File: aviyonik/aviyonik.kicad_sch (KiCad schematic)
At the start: 0 parts

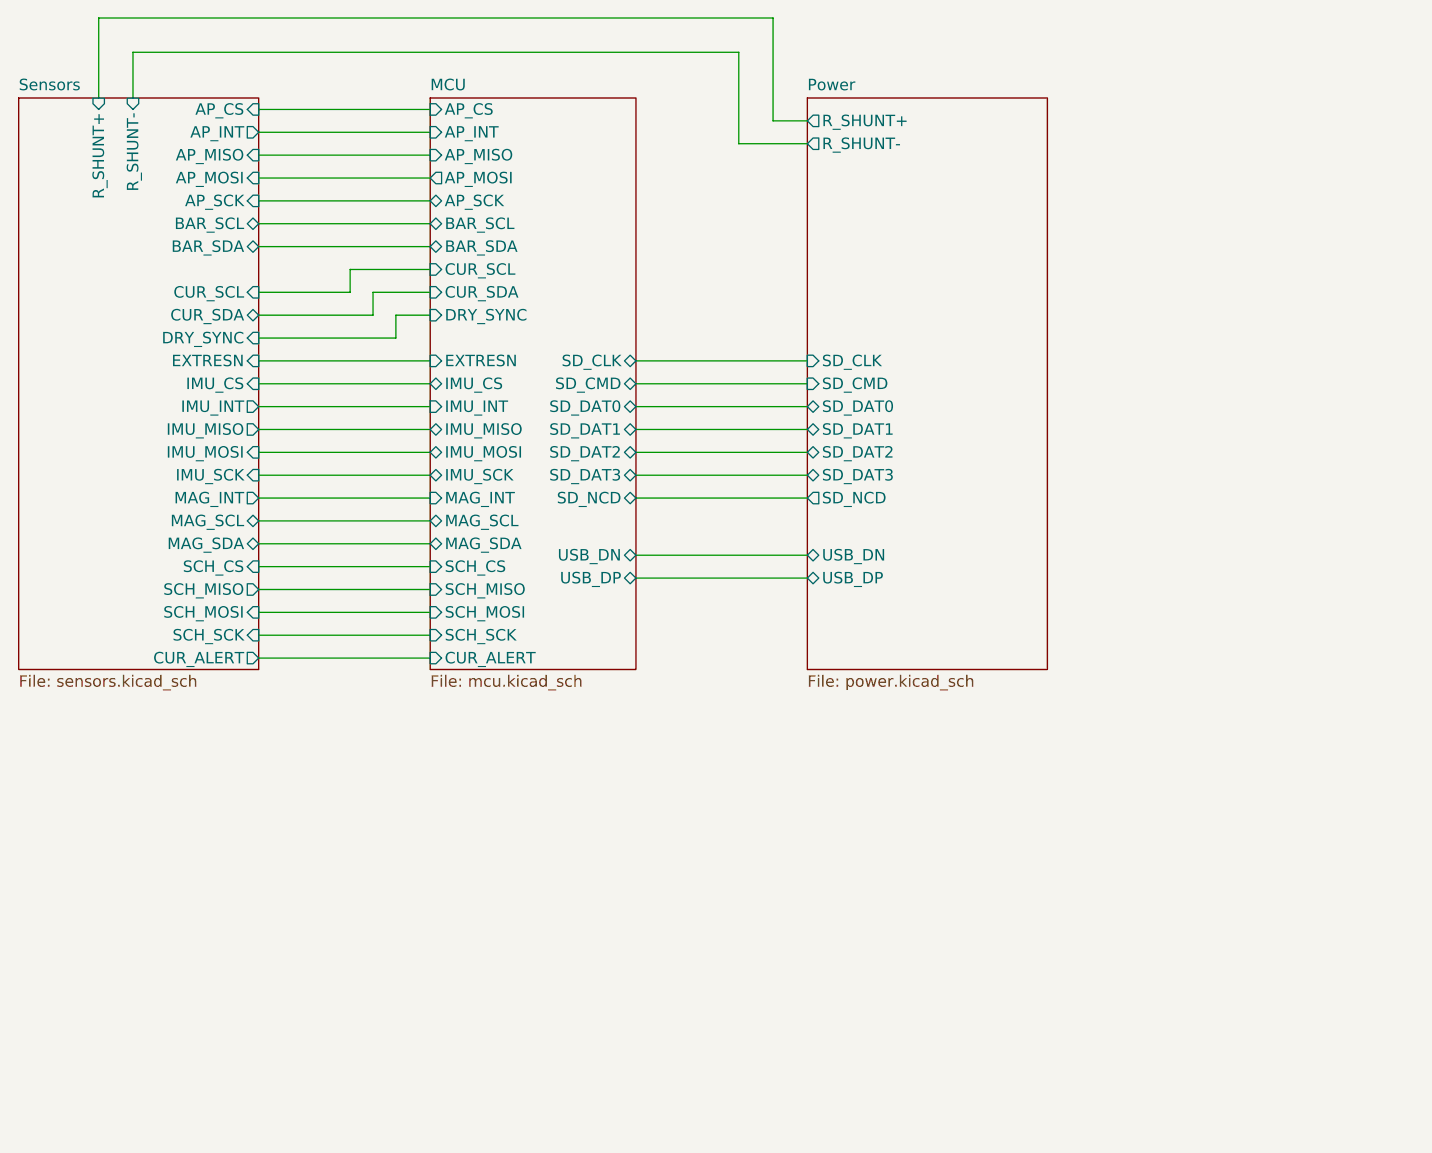
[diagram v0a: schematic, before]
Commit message: revision
connectors have been revisioned
3.3 to 1.8 ldo's have been added to imu's
5 to 3.3v ldo have been changed
i2c and uart connectors have been added for gps and pitot tube connections
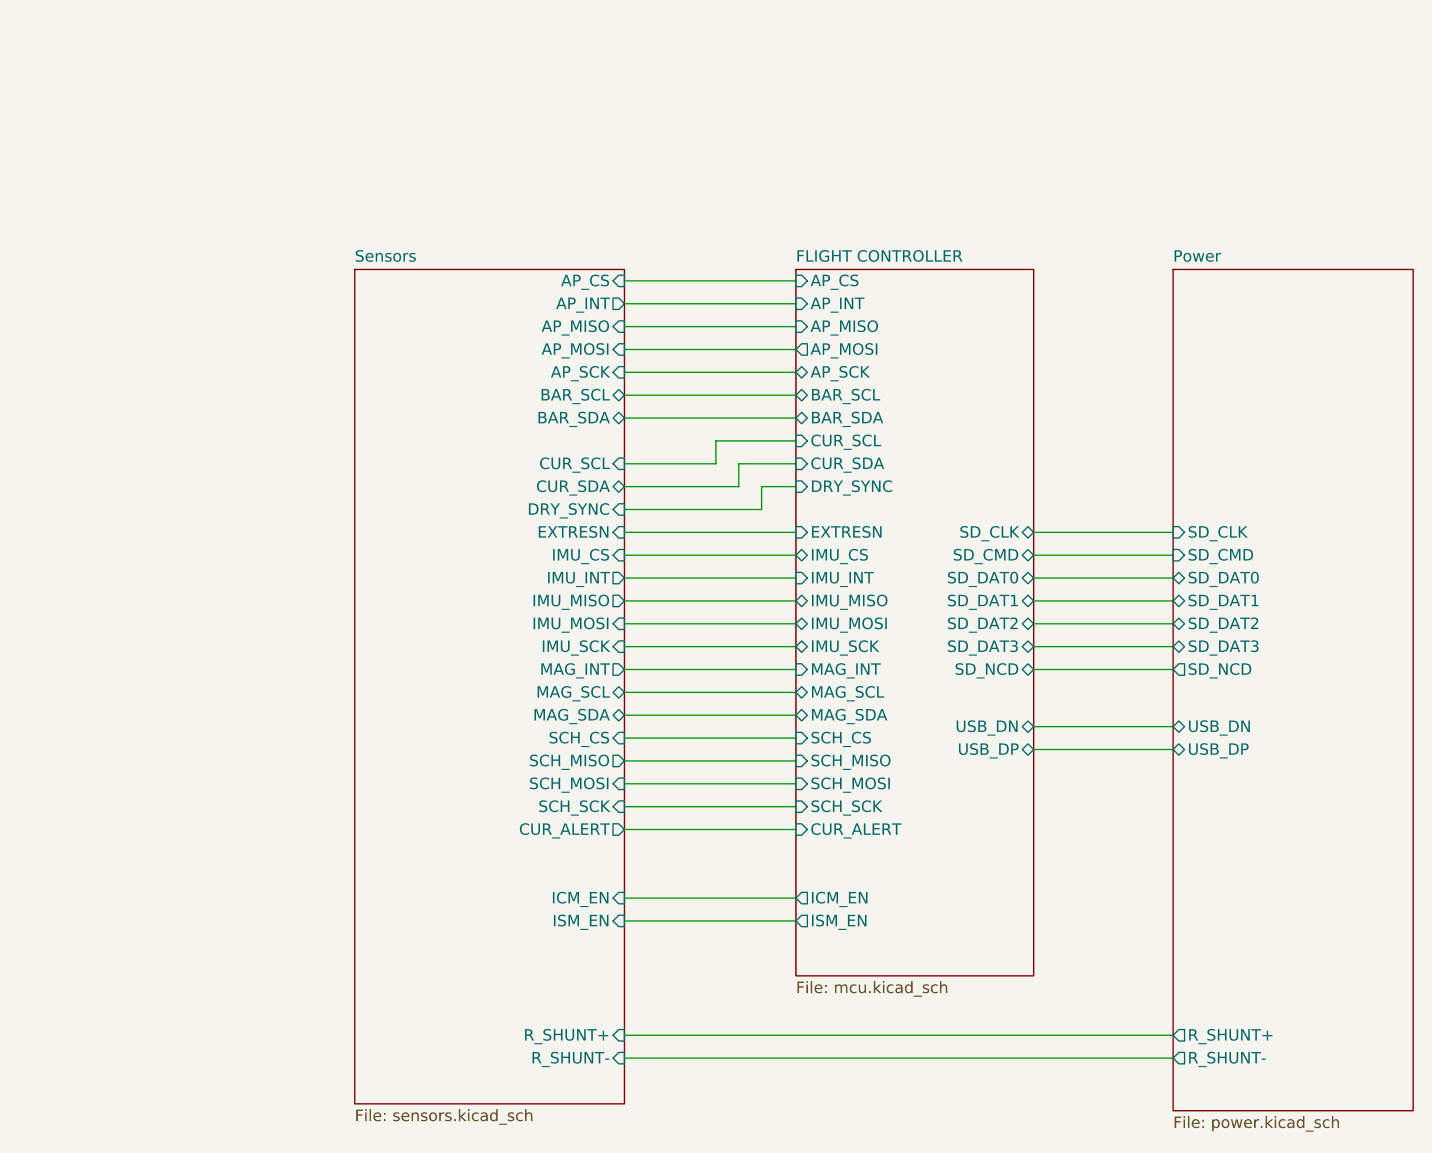
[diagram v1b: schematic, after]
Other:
- sheet MCU renamed FLIGHT CONTROLLER
- sheet FLIGHT CONTROLLER ports: added ICM_EN, ISM_EN; removed none
- sheet Sensors ports: added ICM_EN, ISM_EN; removed none
